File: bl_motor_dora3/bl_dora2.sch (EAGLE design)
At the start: 93 parts

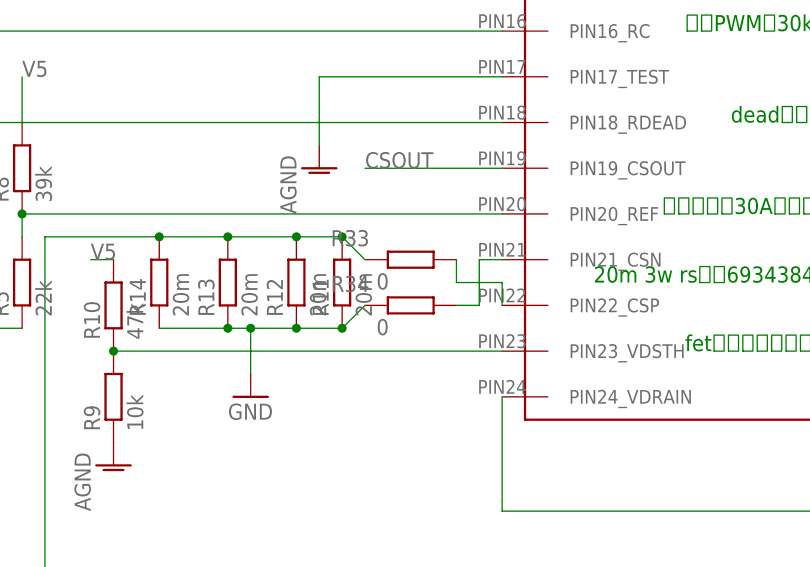
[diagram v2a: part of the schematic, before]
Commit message: 配線修正
シャントの配線をしっかり切り分ける。
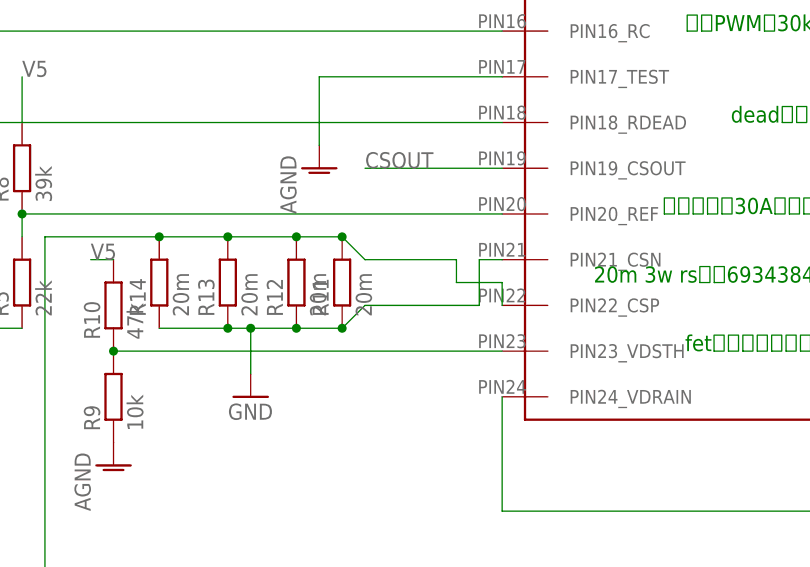
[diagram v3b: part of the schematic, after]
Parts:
- removed R33, R34: 0, user:1608REG
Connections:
- removed net N$10: R33.2, U$1.PIN22_CSP
- removed net N$20: R34.2, U$1.PIN21_CSN
- net GND: now also U$1.PIN21_CSN; no longer R34.1
- net N$40: now also U$1.PIN22_CSP; no longer R33.1
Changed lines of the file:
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@@
 <?xml version="1.0" encoding="utf-8"?>
 <!DOCTYPE eagle SYSTEM "eagle.dtd">
-<eagle version="9.4.2">
+<eagle version="9.5.2">
 <drawing>
 <settings>
@@
 <part name="C17" library="rcl" library_urn="urn:adsk.eagle:library:334" deviceset="C-EU" device="C2012" package3d_urn="urn:adsk.eagle:package:23625/2" value="5n"/>
 <part name="C18" library="rcl" library_urn="urn:adsk.eagle:library:334" deviceset="C-EU" device="C2012" package3d_urn="urn:adsk.eagle:package:23625/2" value="5n"/>
-<part name="R33" library="user" deviceset="1608REG" device="" value="0"/>
-<part name="R34" library="user" deviceset="1608REG" device="" value="0"/>
 <part name="U$20" library="user" deviceset="ES3BB13F" device=""/>
 <part name="U$21" library="user" deviceset="ES3BB13F" device=""/>
@@
 <attribute name="VALUE" x="367.284" y="112.141" size="1.778" layer="96"/>
 </instance>
-<instance part="R33" gate="G$1" x="10.16" y="27.94" smashed="yes">
-<attribute name="NAME" x="1.27" y="29.4386" size="1.778" layer="95"/>
-<attribute name="VALUE" x="6.35" y="24.638" size="1.778" layer="96"/>
-</instance>
-<instance part="R34" gate="G$1" x="10.16" y="22.86" smashed="yes">
-<attribute name="NAME" x="1.27" y="24.3586" size="1.778" layer="95"/>
-<attribute name="VALUE" x="6.35" y="19.558" size="1.778" layer="96"/>
-</instance>
 <instance part="U$20" gate="G$1" x="330.2" y="116.84" smashed="yes">
 <attribute name="NAME" x="328.8284" y="114.3" size="1.778" layer="95" rot="R90"/>
@@
 <pinref part="GND2" gate="1" pin="GND"/>
 <junction x="2.54" y="20.32"/>
-<pinref part="R34" gate="G$1" pin="1"/>
 <wire x1="2.54" y1="20.32" x2="5.08" y2="22.86" width="0.1524" layer="91"/>
+<wire x1="17.78" y1="22.86" x2="17.78" y2="27.94" width="0.1524" layer="91"/>
+<pinref part="U$1" gate="G$1" pin="PIN21_CSN"/>
+<wire x1="17.78" y1="27.94" x2="20.32" y2="27.94" width="0.1524" layer="91"/>
+<wire x1="17.78" y1="22.86" x2="5.08" y2="22.86" width="0.1524" layer="91"/>
 </segment>
 <segment>
@@
 <wire x1="398.78" y1="71.12" x2="388.62" y2="71.12" width="0.1524" layer="91"/>
 <junction x="388.62" y="71.12"/>
-</segment>
-</net>
-<net name="N$10" class="0">
-<segment>
-<pinref part="R33" gate="G$1" pin="2"/>
-<wire x1="15.24" y1="27.94" x2="15.24" y2="25.4" width="0.1524" layer="91"/>
-<pinref part="U$1" gate="G$1" pin="PIN22_CSP"/>
-<wire x1="15.24" y1="25.4" x2="20.32" y2="25.4" width="0.1524" layer="91"/>
-<wire x1="20.32" y1="25.4" x2="20.32" y2="22.86" width="0.1524" layer="91"/>
-</segment>
-</net>
-<net name="N$20" class="0">
-<segment>
-<pinref part="R34" gate="G$1" pin="2"/>
-<wire x1="15.24" y1="22.86" x2="17.78" y2="22.86" width="0.1524" layer="91"/>
-<wire x1="17.78" y1="22.86" x2="17.78" y2="27.94" width="0.1524" layer="91"/>
-<pinref part="U$1" gate="G$1" pin="PIN21_CSN"/>
-<wire x1="17.78" y1="27.94" x2="20.32" y2="27.94" width="0.1524" layer="91"/>
 </segment>
 </net>
@@
 <wire x1="414.02" y1="48.26" x2="416.56" y2="45.72" width="0.1524" layer="91"/>
 <junction x="416.56" y="45.72"/>
-<pinref part="R33" gate="G$1" pin="1"/>
 <wire x1="2.54" y1="30.48" x2="5.08" y2="27.94" width="0.1524" layer="91"/>
 <junction x="2.54" y="30.48"/>
@@
 <wire x1="447.04" y1="45.72" x2="429.26" y2="45.72" width="0.1524" layer="91"/>
 <junction x="429.26" y="45.72"/>
-</segment>
-</net>
+<wire x1="15.24" y1="27.94" x2="15.24" y2="25.4" width="0.1524" layer="91"/>
+<pinref part="U$1" gate="G$1" pin="PIN22_CSP"/>
+<wire x1="15.24" y1="25.4" x2="20.32" y2="25.4" width="0.1524" layer="91"/>
+<wire x1="20.32" y1="25.4" x2="20.32" y2="22.86" width="0.1524" layer="91"/>
+<wire x1="5.08" y1="27.94" x2="15.24" y2="27.94" width="0.1524" layer="91"/>
+</segment>
+</net>

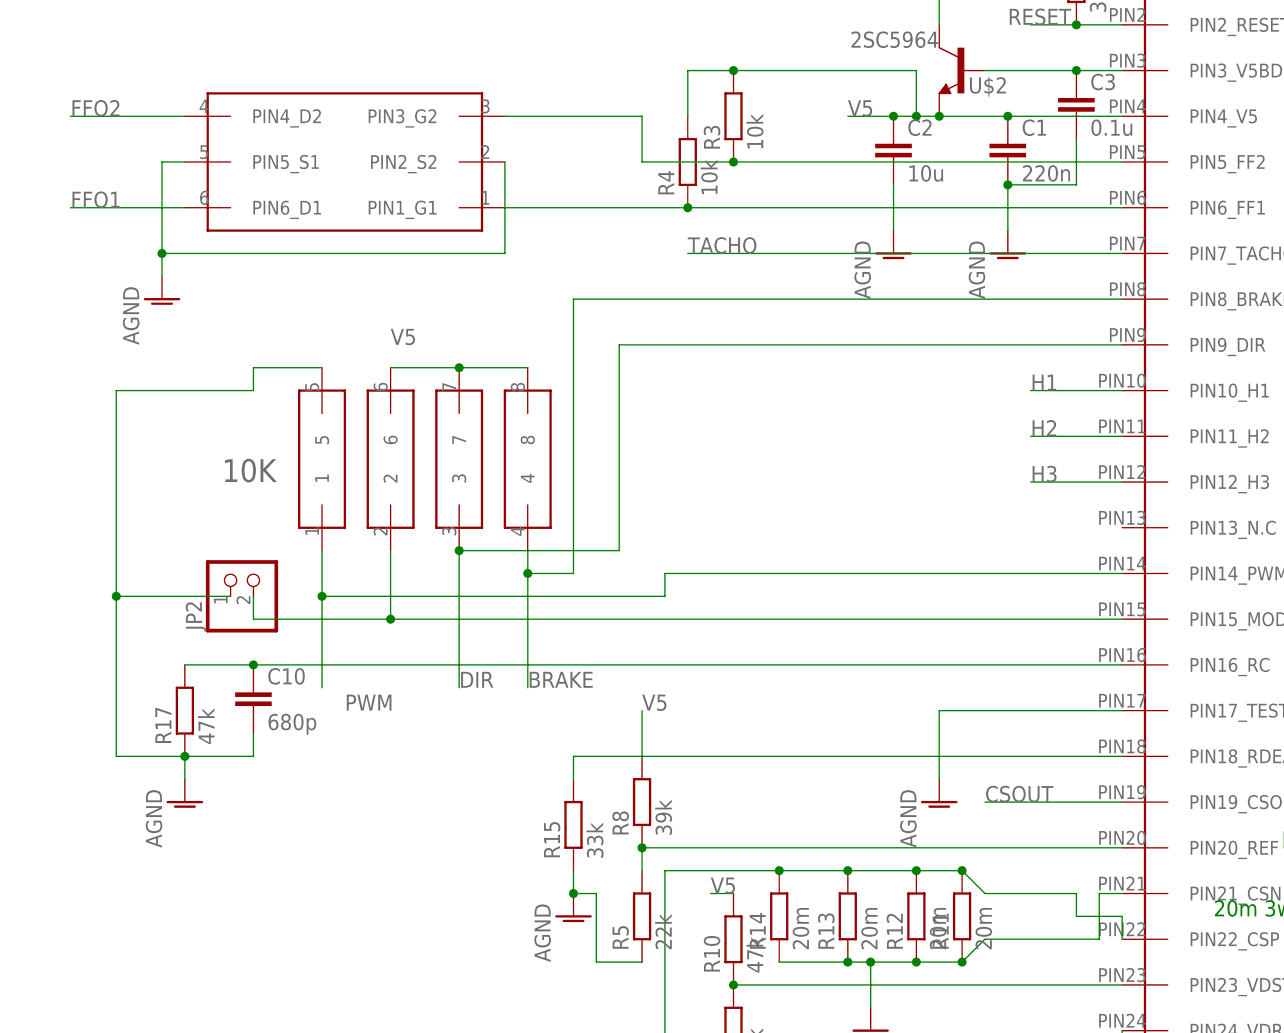
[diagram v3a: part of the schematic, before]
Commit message: 完成品
配線の修正などをおこなった
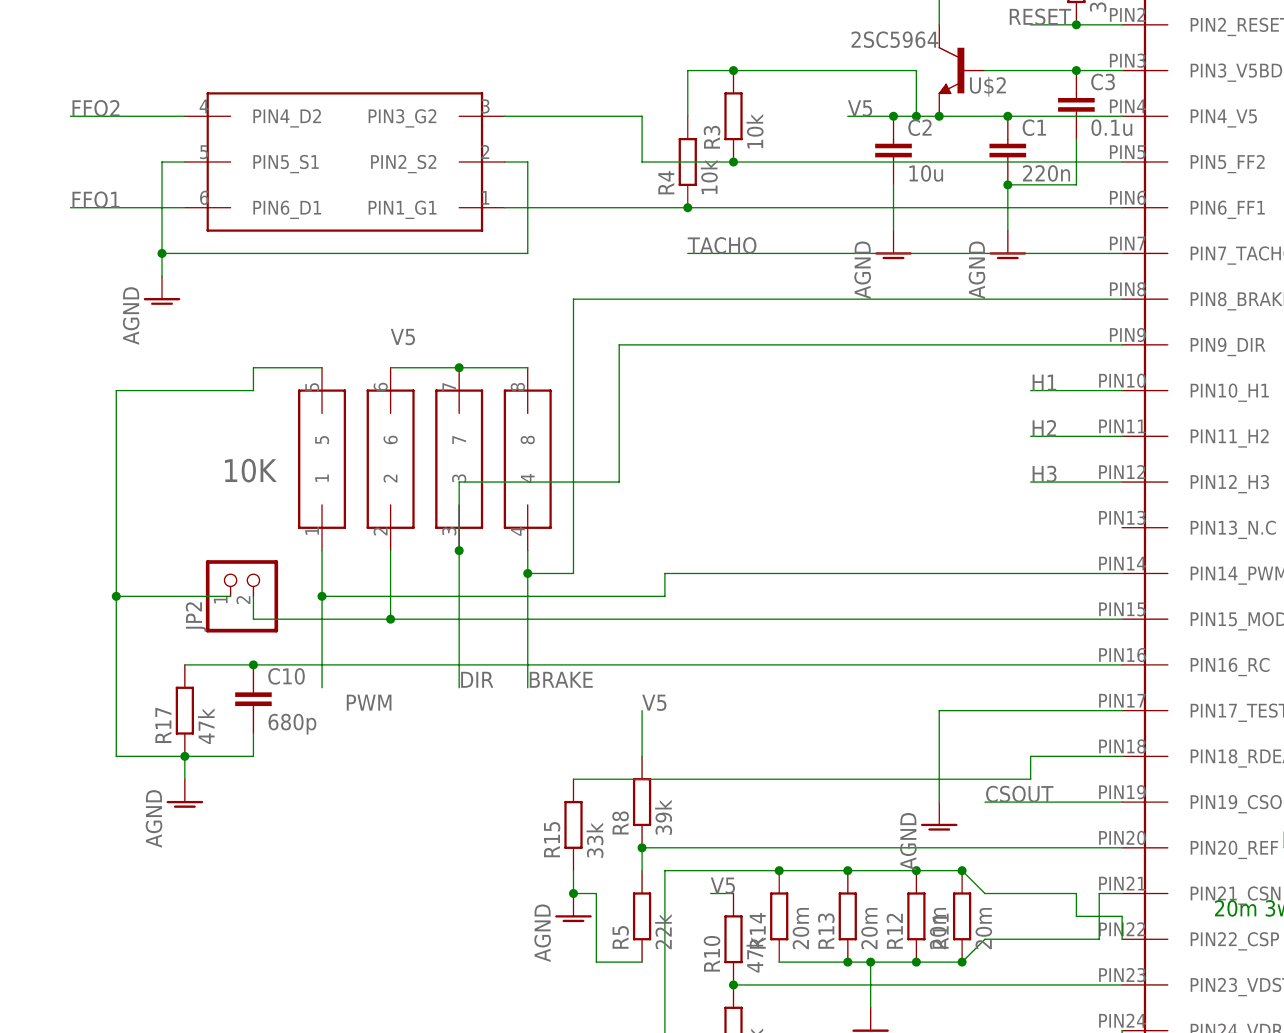
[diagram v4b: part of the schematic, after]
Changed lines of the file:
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@@
 <?xml version="1.0" encoding="utf-8"?>
 <!DOCTYPE eagle SYSTEM "eagle.dtd">
-<eagle version="9.5.2">
+<eagle version="9.4.2">
 <drawing>
 <settings>
@@
 <attribute name="VALUE" x="-88.9" y="88.9" size="1.778" layer="96" rot="R90"/>
 </instance>
-<instance part="AGND6" gate="VR1" x="0" y="38.1" smashed="yes">
-<attribute name="VALUE" x="-2.54" y="33.02" size="1.778" layer="96" rot="R90"/>
+<instance part="AGND6" gate="VR1" x="0" y="35.56" smashed="yes">
+<attribute name="VALUE" x="-2.54" y="30.48" size="1.778" layer="96" rot="R90"/>
 </instance>
 <instance part="R8" gate="G$1" x="-33.02" y="38.1" smashed="yes" rot="R90">
@@
 <wire x1="-83.82" y1="109.22" x2="-86.36" y2="109.22" width="0.1524" layer="91"/>
 <wire x1="-86.36" y1="109.22" x2="-86.36" y2="99.06" width="0.1524" layer="91"/>
-<pinref part="U$3" gate="G$1" pin="PIN2_S2"/>
 <wire x1="-86.36" y1="99.06" x2="-86.36" y2="96.52" width="0.1524" layer="91"/>
-<wire x1="-48.26" y1="109.22" x2="-48.26" y2="99.06" width="0.1524" layer="91"/>
-<wire x1="-48.26" y1="99.06" x2="-86.36" y2="99.06" width="0.1524" layer="91"/>
+<wire x1="-45.72" y1="99.06" x2="-86.36" y2="99.06" width="0.1524" layer="91"/>
 <junction x="-86.36" y="99.06"/>
 <pinref part="AGND4" gate="VR1" pin="AGND"/>
+<pinref part="U$3" gate="G$1" pin="PIN2_S2"/>
+<wire x1="-48.26" y1="109.22" x2="-45.72" y2="109.22" width="0.1524" layer="91"/>
+<wire x1="-45.72" y1="109.22" x2="-45.72" y2="99.06" width="0.1524" layer="91"/>
 </segment>
 <segment>
 <pinref part="U$1" gate="G$1" pin="PIN17_TEST"/>
 <wire x1="20.32" y1="48.26" x2="0" y2="48.26" width="0.1524" layer="91"/>
-<wire x1="0" y1="48.26" x2="0" y2="40.64" width="0.1524" layer="91"/>
+<wire x1="0" y1="48.26" x2="0" y2="38.1" width="0.1524" layer="91"/>
 <pinref part="AGND6" gate="VR1" pin="AGND"/>
 </segment>
@@
 <pinref part="U$1" gate="G$1" pin="PIN9_DIR"/>
 <wire x1="20.32" y1="88.9" x2="-35.56" y2="88.9" width="0.1524" layer="91"/>
-<wire x1="-35.56" y1="88.9" x2="-35.56" y2="66.04" width="0.1524" layer="91"/>
+<wire x1="-35.56" y1="88.9" x2="-35.56" y2="73.66" width="0.1524" layer="91"/>
+<wire x1="-35.56" y1="73.66" x2="-53.34" y2="73.66" width="0.1524" layer="91"/>
 <pinref part="U$5" gate="G$1" pin="3"/>
 <wire x1="-53.34" y1="66.04" x2="-53.34" y2="50.8" width="0.1524" layer="91"/>
 <label x="-53.34" y="50.8" size="1.778" layer="95"/>
-<wire x1="-35.56" y1="66.04" x2="-53.34" y2="66.04" width="0.1524" layer="91"/>
+<wire x1="-53.34" y1="73.66" x2="-53.34" y2="66.04" width="0.1524" layer="91"/>
 <junction x="-53.34" y="66.04"/>
 </segment>
@@
 <pinref part="U$1" gate="G$1" pin="PIN43_CP2"/>
 <wire x1="134.62" y1="35.56" x2="134.62" y2="38.1" width="0.1524" layer="91"/>
-</segment>
-</net>
-<net name="N$15" class="0">
-<segment>
-<pinref part="U$1" gate="G$1" pin="PIN18_RDEAD"/>
-<pinref part="R15" gate="G$1" pin="2"/>
-<wire x1="20.32" y1="43.18" x2="-40.64" y2="43.18" width="0.1524" layer="91"/>
-<wire x1="-40.64" y1="43.18" x2="-40.64" y2="40.64" width="0.1524" layer="91"/>
 </segment>
 </net>
@@
 </segment>
 </net>
+<net name="N$4" class="0">
+<segment>
+<pinref part="R15" gate="G$1" pin="2"/>
+<wire x1="-40.64" y1="40.64" x2="10.16" y2="40.64" width="0.1524" layer="91"/>
+<wire x1="10.16" y1="40.64" x2="10.16" y2="43.18" width="0.1524" layer="91"/>
+<pinref part="U$1" gate="G$1" pin="PIN18_RDEAD"/>
+<wire x1="10.16" y1="43.18" x2="20.32" y2="43.18" width="0.1524" layer="91"/>
+</segment>
+</net>

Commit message: スケマチックの抵抗の値がおかしかった
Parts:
- R26, R30, R31, R32, R6, R7: value 47 -> 22
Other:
- note added: "22Ωの抵抗器は1206の0.66W。rs品番721-9680"
- note added: "F_C*のコンデンサは0.33uFのフィルムコンデンサ"
- note removed: "47Ωの抵抗器は1206の0.66W。rs品番721-9715"
- note removed: "F_C*のコンデンサは0.1uFのフィルムコンデンサ"
- moved on the sheet: R10, R9
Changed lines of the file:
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@@
 <part name="U$27" library="user" deviceset="ES3BB13F" device=""/>
 <part name="U$28" library="user" deviceset="ES3BB13F" device=""/>
-<part name="R6" library="rcl" library_urn="urn:adsk.eagle:library:334" deviceset="R-EU_" device="R1206" package3d_urn="urn:adsk.eagle:package:23540/2" value="47"/>
-<part name="R7" library="rcl" library_urn="urn:adsk.eagle:library:334" deviceset="R-EU_" device="R1206" package3d_urn="urn:adsk.eagle:package:23540/2" value="47"/>
-<part name="R26" library="rcl" library_urn="urn:adsk.eagle:library:334" deviceset="R-EU_" device="R1206" package3d_urn="urn:adsk.eagle:package:23540/2" value="47"/>
-<part name="R30" library="rcl" library_urn="urn:adsk.eagle:library:334" deviceset="R-EU_" device="R1206" package3d_urn="urn:adsk.eagle:package:23540/2" value="47"/>
-<part name="R31" library="rcl" library_urn="urn:adsk.eagle:library:334" deviceset="R-EU_" device="R1206" package3d_urn="urn:adsk.eagle:package:23540/2" value="47"/>
-<part name="R32" library="rcl" library_urn="urn:adsk.eagle:library:334" deviceset="R-EU_" device="R1206" package3d_urn="urn:adsk.eagle:package:23540/2" value="47"/>
+<part name="R6" library="rcl" library_urn="urn:adsk.eagle:library:334" deviceset="R-EU_" device="R1206" package3d_urn="urn:adsk.eagle:package:23540/2" value="22"/>
+<part name="R7" library="rcl" library_urn="urn:adsk.eagle:library:334" deviceset="R-EU_" device="R1206" package3d_urn="urn:adsk.eagle:package:23540/2" value="22"/>
+<part name="R26" library="rcl" library_urn="urn:adsk.eagle:library:334" deviceset="R-EU_" device="R1206" package3d_urn="urn:adsk.eagle:package:23540/2" value="22"/>
+<part name="R30" library="rcl" library_urn="urn:adsk.eagle:library:334" deviceset="R-EU_" device="R1206" package3d_urn="urn:adsk.eagle:package:23540/2" value="22"/>
+<part name="R31" library="rcl" library_urn="urn:adsk.eagle:library:334" deviceset="R-EU_" device="R1206" package3d_urn="urn:adsk.eagle:package:23540/2" value="22"/>
+<part name="R32" library="rcl" library_urn="urn:adsk.eagle:library:334" deviceset="R-EU_" device="R1206" package3d_urn="urn:adsk.eagle:package:23540/2" value="22"/>
 </parts>
 <sheets>
@@
 <text x="91.44" y="137.16" size="1.778" layer="91">fetを変えた場合はそのfetのゲート容量によってブートストラップコンデンサを変えること</text>
 <text x="393.7" y="200.66" size="1.778" layer="91">rs品番843-2168の820uFのコンデンサ</text>
-<text x="396.24" y="27.94" size="1.778" layer="91">F_C*のコンデンサは0.1uFのフィルムコンデンサ</text>
+<text x="396.24" y="27.94" size="1.778" layer="91">F_C*のコンデンサは0.33uFのフィルムコンデンサ</text>
 <text x="396.24" y="22.86" size="1.778" layer="91">fetにSQD50034ELを使う。同じto252</text>
 <text x="38.1" y="33.02" size="1.778" layer="91">電流制限は30Aに設定されている。refの抵抗比を変えることで変更可</text>
 <text x="40.64" y="17.78" size="1.778" layer="91">fetのドレインソース間がオン時に1Vを超えたら短絡とみなされる</text>
-<text x="396.24" y="17.78" size="1.778" layer="91">47Ωの抵抗器は1206の0.66W。rs品番721-9715</text>
+<text x="396.24" y="17.78" size="1.778" layer="91">22Ωの抵抗器は1206の0.66W。rs品番721-9680</text>
 </plain>
 <instances>
@@
 <attribute name="VALUE" x="-29.718" y="34.29" size="1.778" layer="96" rot="R90"/>
 </instance>
-<instance part="R9" gate="G$1" x="-22.86" y="12.7" smashed="yes" rot="R90">
-<attribute name="NAME" x="-24.3586" y="8.89" size="1.778" layer="95" rot="R90"/>
-<attribute name="VALUE" x="-19.558" y="8.89" size="1.778" layer="96" rot="R90"/>
-</instance>
-<instance part="R10" gate="G$1" x="-22.86" y="22.86" smashed="yes" rot="R90">
-<attribute name="NAME" x="-24.3586" y="19.05" size="1.778" layer="95" rot="R90"/>
-<attribute name="VALUE" x="-19.558" y="19.05" size="1.778" layer="96" rot="R90"/>
-</instance>
-<instance part="AGND7" gate="VR1" x="-22.86" y="5.08" smashed="yes">
-<attribute name="VALUE" x="-25.4" y="0" size="1.778" layer="96" rot="R90"/>
+<instance part="R9" gate="G$1" x="-25.4" y="12.7" smashed="yes" rot="R90">
+<attribute name="NAME" x="-26.8986" y="8.89" size="1.778" layer="95" rot="R90"/>
+<attribute name="VALUE" x="-22.098" y="8.89" size="1.778" layer="96" rot="R90"/>
+</instance>
+<instance part="R10" gate="G$1" x="-25.4" y="22.86" smashed="yes" rot="R90">
+<attribute name="NAME" x="-26.8986" y="19.05" size="1.778" layer="95" rot="R90"/>
+<attribute name="VALUE" x="-22.098" y="19.05" size="1.778" layer="96" rot="R90"/>
+</instance>
+<instance part="AGND7" gate="VR1" x="-25.4" y="5.08" smashed="yes">
+<attribute name="VALUE" x="-27.94" y="0" size="1.778" layer="96" rot="R90"/>
 </instance>
 <instance part="R11" gate="G$1" x="2.54" y="25.4" smashed="yes" rot="R90">
@@
 <segment>
 <pinref part="R10" gate="G$1" pin="2"/>
-<wire x1="-22.86" y1="27.94" x2="-25.4" y2="27.94" width="0.1524" layer="91"/>
-<label x="-25.4" y="27.94" size="1.778" layer="95"/>
+<wire x1="-25.4" y1="27.94" x2="-27.94" y2="27.94" width="0.1524" layer="91"/>
+<label x="-27.94" y="27.94" size="1.778" layer="95"/>
 </segment>
 <segment>
@@
 <segment>
 <pinref part="U$1" gate="G$1" pin="PIN23_VDSTH"/>
-<wire x1="20.32" y1="17.78" x2="-22.86" y2="17.78" width="0.1524" layer="91"/>
+<wire x1="20.32" y1="17.78" x2="-25.4" y2="17.78" width="0.1524" layer="91"/>
 <pinref part="R9" gate="G$1" pin="2"/>
 <pinref part="R10" gate="G$1" pin="1"/>
-<junction x="-22.86" y="17.78"/>
-</segment>
-</net>
+<junction x="-25.4" y="17.78"/>
+</segment>
+</net>
